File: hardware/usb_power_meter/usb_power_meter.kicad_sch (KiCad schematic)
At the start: 22 parts, among them U1 nRF52833-QDxx, U2 INA226, X1 32Mhz crystal, X2 32.768kHz crystal

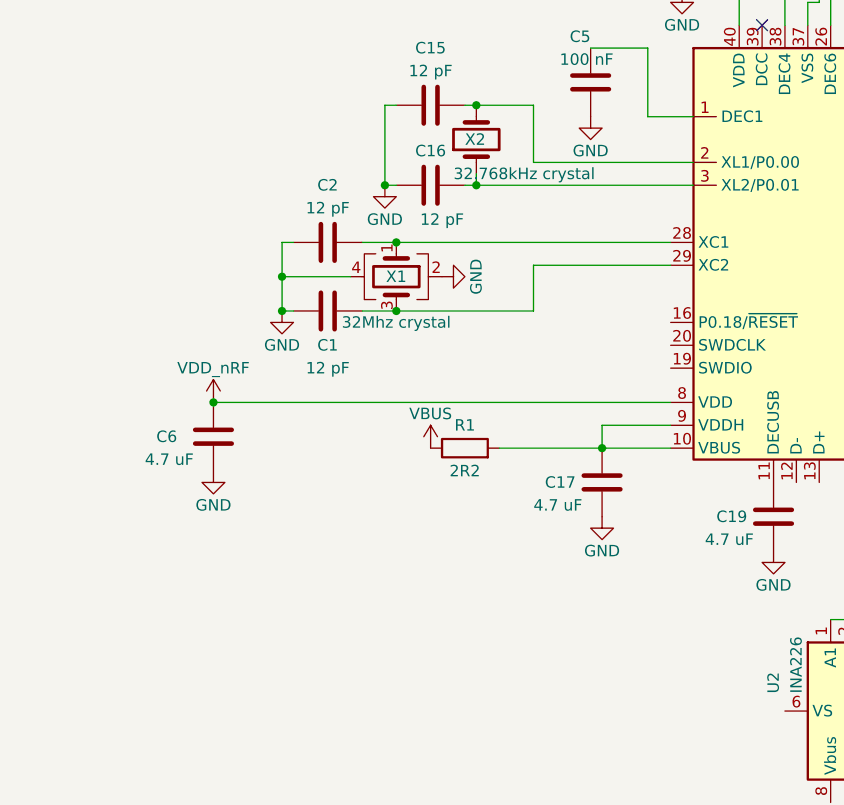
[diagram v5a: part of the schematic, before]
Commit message: Add debugging connector
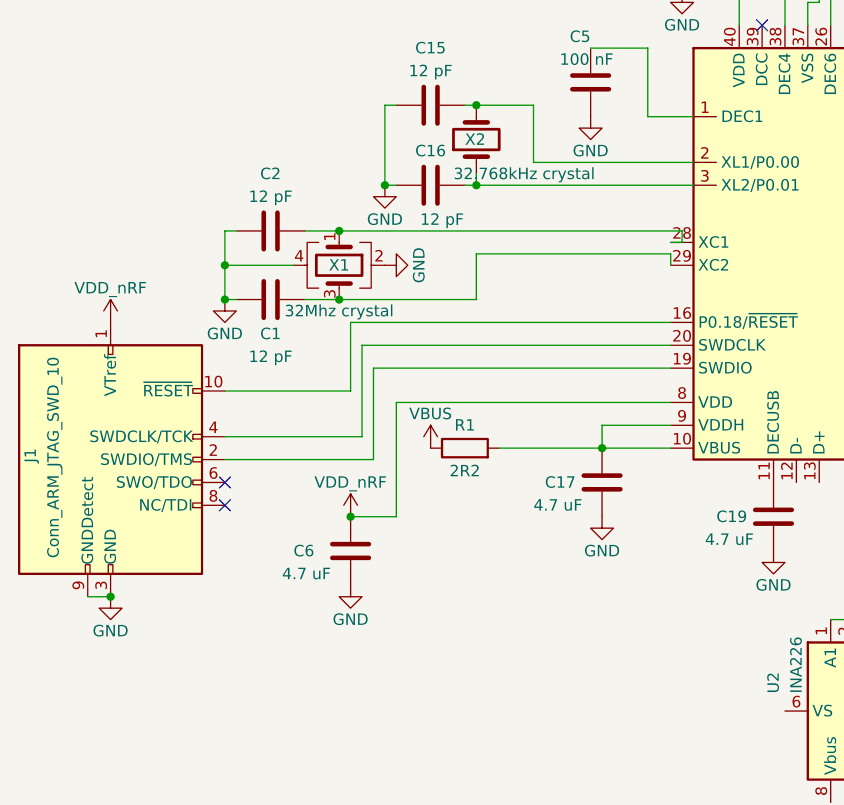
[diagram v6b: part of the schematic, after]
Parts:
- added J1: Conn_ARM_JTAG_SWD_10, Connector_PinHeader_1.27mm:PinHeader_2x05_P1.27mm_Vertical_SMD, symbol Connector:Conn_ARM_JTAG_SWD_10
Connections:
- net GND: now also J1.3 (GND), J1.5 (GND), J1.9 (GNDDetect)
- net VDD: now also J1.1 (VTref)
- net at U1.16 (P0.18/~{RESET}): now also J1.10 (~{RESET})
- net at U1.19 (SWDIO): now also J1.2 (SWDIO/TMS)
- net at U1.20 (SWDCLK): now also J1.4 (SWDCLK/TCK)
- no-connect marks 1 -> 3
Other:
- moved on the sheet: C1, C2, C6, X1

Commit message: Switch most capacitors to LCSC basic parts instead of extended ones.
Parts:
- C1, C12, C13, C15, C16, C2: LCSC type (none) -> Basic
- C10: LCSC C126492 -> C1546; LCSC type (none) -> Basic
- C11, C5, C7: LCSC C71629 -> C1525; LCSC type (none) -> Basic
- C17, C19, C6: LCSC C71631 -> C19666; LCSC type (none) -> Basic
- C3: LCSC C72134 -> C1550; LCSC type (none) -> Basic
- C4: LCSC type (none) -> Extended
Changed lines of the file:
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@@
+      (effects (font (size 1.27 1.27)) hide)
+    )
+    (property "LCSC type" "Basic" (at 73.66 102.87 0)
       (effects (font (size 1.27 1.27)) hide)
     )
@@
     )
     (property "LCSC" "C1547" (at 91.44 88.9 0)
+      (effects (font (size 1.27 1.27)) hide)
+    )
+    (property "LCSC type" "Basic" (at 91.44 88.9 0)
       (effects (font (size 1.27 1.27)) hide)
     )
@@
       (effects (font (size 1.27 1.27)) hide)
     )
-    (property "LCSC" "C71631" (at 129.54 134.62 0)
+    (property "LCSC" "C19666" (at 129.54 134.62 0)
+      (effects (font (size 1.27 1.27)) hide)
+    )
+    (property "LCSC type" "Basic" (at 129.54 134.62 0)
       (effects (font (size 1.27 1.27)) hide)
     )
@@
       (effects (font (size 1.27 1.27)) hide)
     )
-    (property "LCSC" "C71631" (at 82.55 138.43 0)
+    (property "LCSC" "C19666" (at 82.55 138.43 0)
+      (effects (font (size 1.27 1.27)) hide)
+    )
+    (property "LCSC type" "Basic" (at 82.55 138.43 0)
       (effects (font (size 1.27 1.27)) hide)
     )
@@
       (effects (font (size 1.27 1.27)) hide)
     )
+    (property "LCSC type" "Basic" (at 119.38 72.39 0)
+      (effects (font (size 1.27 1.27)) hide)
+    )
     (pin "1")
     (pin "2")
@@
       (effects (font (size 1.27 1.27)) hide)
     )
-    (property "LCSC" "C71631" (at 110.49 130.81 0)
+    (property "LCSC" "C19666" (at 110.49 130.81 0)
+      (effects (font (size 1.27 1.27)) hide)
+    )
+    (property "LCSC type" "Basic" (at 110.49 130.81 0)
       (effects (font (size 1.27 1.27)) hide)
     )
@@
       (effects (font (size 1.27 1.27)) hide)
     )
-    (property "LCSC" "C126492" (at 161.29 74.93 0)
+    (property "LCSC" "C1546" (at 161.29 74.93 0)
+      (effects (font (size 1.27 1.27)) hide)
+    )
+    (property "LCSC type" "Basic" (at 161.29 74.93 0)
       (effects (font (size 1.27 1.27)) hide)
     )
@@
     )
     (property "LCSC" "C15849" (at 133.35 67.31 0)
+      (effects (font (size 1.27 1.27)) hide)
+    )
+    (property "LCSC type" "Basic" (at 133.35 67.31 0)
       (effects (font (size 1.27 1.27)) hide)
     )
@@
       (effects (font (size 1.27 1.27)) hide)
     )
-    (property "LCSC" "C71629" (at 146.05 66.04 0)
+    (property "LCSC" "C1525" (at 146.05 66.04 0)
+      (effects (font (size 1.27 1.27)) hide)
+    )
+    (property "LCSC type" "Basic" (at 146.05 66.04 0)
       (effects (font (size 1.27 1.27)) hide)
     )
@@
     )
     (property "LCSC" "C1547" (at 73.66 110.49 0)
+      (effects (font (size 1.27 1.27)) hide)
+    )
+    (property "LCSC type" "Basic" (at 73.66 110.49 0)
       (effects (font (size 1.27 1.27)) hide)
     )
@@
       (effects (font (size 1.27 1.27)) hide)
     )
+    (property "LCSC type" "Basic" (at 91.44 97.79 0)
+      (effects (font (size 1.27 1.27)) hide)
+    )
     (pin "1")
     (pin "2")
@@
       (effects (font (size 1.27 1.27)) hide)
     )
+    (property "LCSC type" "Extended" (at 198.12 116.84 0)
+      (effects (font (size 1.27 1.27)) hide)
+    )
     (pin "1")
     (pin "2")
@@
       (effects (font (size 1.27 1.27)) hide)
     )
-    (property "LCSC" "C71629" (at 152.4 66.04 0)
+    (property "LCSC" "C1525" (at 152.4 66.04 0)
+      (effects (font (size 1.27 1.27)) hide)
+    )
+    (property "LCSC type" "Basic" (at 152.4 66.04 0)
       (effects (font (size 1.27 1.27)) hide)
     )
@@
       (effects (font (size 1.27 1.27)) hide)
     )
-    (property "LCSC" "C71629" (at 109.22 86.36 0)
+    (property "LCSC" "C1525" (at 109.22 86.36 0)
+      (effects (font (size 1.27 1.27)) hide)
+    )
+    (property "LCSC type" "Basic" (at 109.22 86.36 0)
       (effects (font (size 1.27 1.27)) hide)
     )
@@
       (effects (font (size 1.27 1.27)) hide)
     )
-    (property "LCSC" "C72134" (at 186.69 116.84 0)
-      (effects (font (size 1.27 1.27)) hide)
-    )
+    (property "LCSC" "C1550" (at 186.69 116.84 0)
+      (effects (font (size 1.27 1.27)) hide)
+    )
+    (property "LCSC type" "Basic" (at 186.69 116.84 0)
+      (effects (font (size 1.27 1.27)) hide)
+    )
